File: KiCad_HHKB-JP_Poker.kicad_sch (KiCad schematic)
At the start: 21 parts, among them SW1 SW_Push, U1 ATmega32U4-MU, U2 PRTR5V0U2X, Y1 16MHz

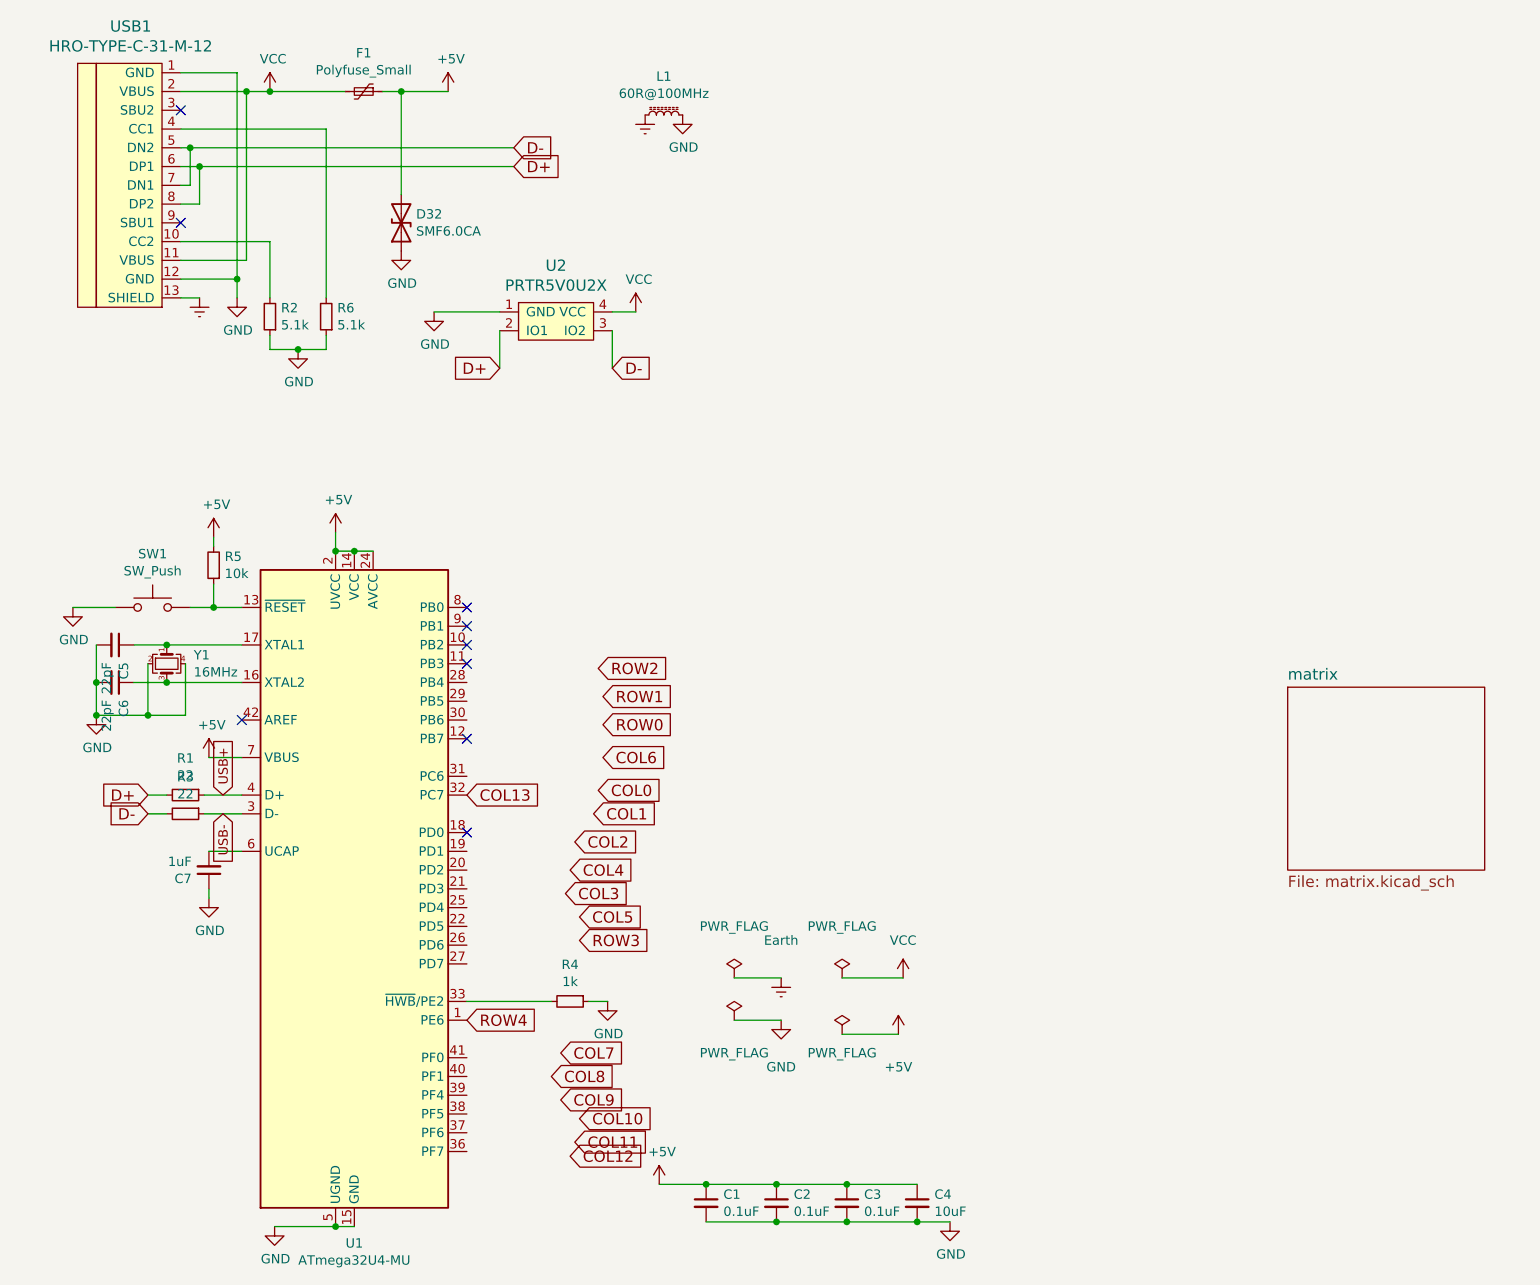
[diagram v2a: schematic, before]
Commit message: 縦（Col）の配線完了
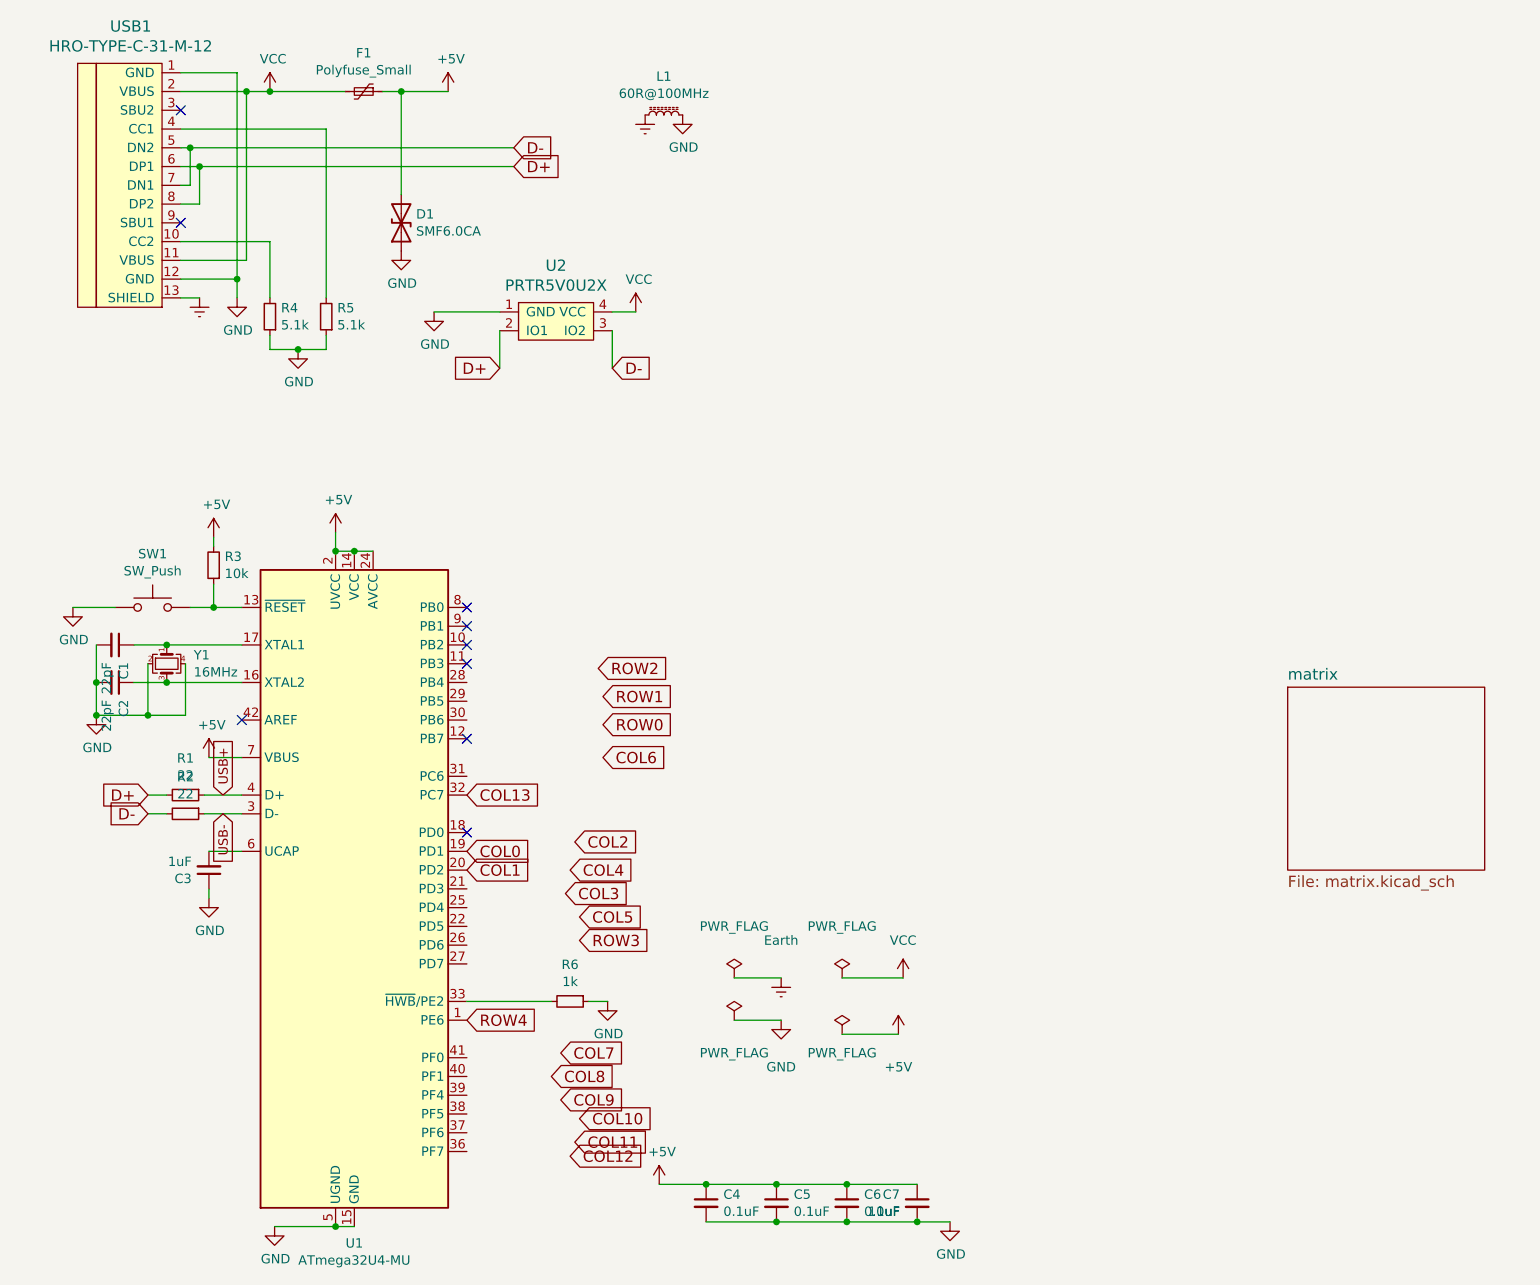
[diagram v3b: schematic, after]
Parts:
- renumbered C5 to C1, C6 to C2, C7 to C3, C1 to C4, C2 to C5, C3 to C6, C4 to C7, D32 to D1, R3 to R2, R5 to R3, R2 to R4, R6 to R5, R4 to R6
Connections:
- net COL0: now also U1.19 (PD1)
- net COL1: now also U1.20 (PD2)

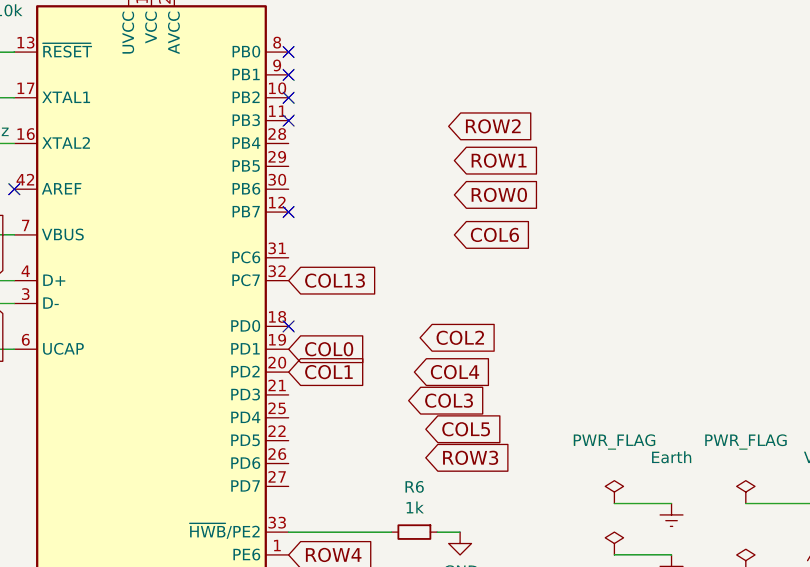
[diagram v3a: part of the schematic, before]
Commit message: key switch 間の配線は完了。これから、Key Switch と MCUを使う
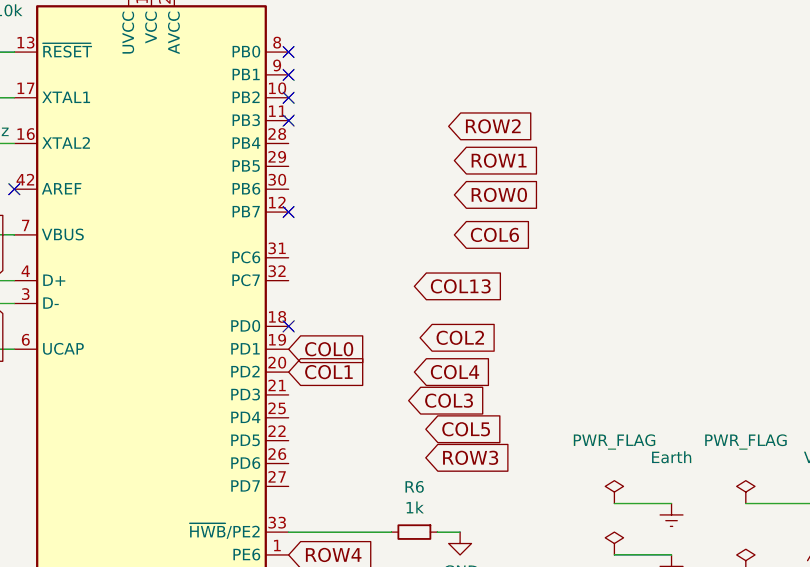
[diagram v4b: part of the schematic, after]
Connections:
- net COL13: no longer U1.32 (PC7)
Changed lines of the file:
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@@
     )
   )
-  (global_label "COL13" (shape input) (at 76.2 124.46 0) (fields_autoplaced)
+  (global_label "COL13" (shape input) (at 90.17 125.095 0) (fields_autoplaced)
     (effects (font (size 1.524 1.524)) (justify left))
-    (property "Intersheet References" "${INTERSHEET_REFS}" (id 0) (at 0 0 0)
+    (property "Intersheet References" "${INTERSHEET_REFS}" (id 0) (at 13.97 0.635 0)
       (effects (font (size 1.27 1.27)) hide)
     )

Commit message: 配線完了（検算はこれから）
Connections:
- net COL10: now also U1.29 (PB5)
- net COL11: now also U1.32 (PC7)
- net COL12: now also U1.31 (PC6)
- net COL13: now also U1.30 (PB6)
- net COL2: now also U1.41 (PF0)
- net COL3: now also U1.40 (PF1)
- net COL4: now also U1.39 (PF4)
- net COL5: now also U1.38 (PF5)
- net COL6: now also U1.37 (PF6)
- net COL7: now also U1.36 (PF7)
- net COL8: now also U1.27 (PD7)
- net COL9: now also U1.28 (PB4)
- net ROW0: now also U1.26 (PD6)
- net ROW1: now also U1.25 (PD4)
- net ROW2: now also U1.22 (PD5)
- net ROW3: now also U1.21 (PD3)
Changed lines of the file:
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@@
     )
   )
-  (global_label "ROW2" (shape input) (at 93.98 107.315 0) (fields_autoplaced)
+  (global_label "ROW2" (shape input) (at 76.2 142.24 0) (fields_autoplaced)
     (effects (font (size 1.524 1.524)) (justify left))
-    (property "Intersheet References" "${INTERSHEET_REFS}" (id 0) (at 17.78 -1.905 0)
+    (property "Intersheet References" "${INTERSHEET_REFS}" (id 0) (at 0 33.02 0)
       (effects (font (size 1.27 1.27)) hide)
     )
   )
-  (global_label "COL6" (shape input) (at 94.615 119.38 0) (fields_autoplaced)
+  (global_label "COL6" (shape input) (at 76.2 170.18 0) (fields_autoplaced)
     (effects (font (size 1.524 1.524)) (justify left))
-    (property "Intersheet References" "${INTERSHEET_REFS}" (id 0) (at 18.415 -2.54 0)
+    (property "Intersheet References" "${INTERSHEET_REFS}" (id 0) (at 0 48.26 0)
       (effects (font (size 1.27 1.27)) hide)
     )
   )
-  (global_label "COL13" (shape input) (at 90.17 125.095 0) (fields_autoplaced)
+  (global_label "COL13" (shape input) (at 76.2 114.3 0) (fields_autoplaced)
     (effects (font (size 1.524 1.524)) (justify left))
-    (property "Intersheet References" "${INTERSHEET_REFS}" (id 0) (at 13.97 0.635 0)
+    (property "Intersheet References" "${INTERSHEET_REFS}" (id 0) (at 0 -10.16 0)
       (effects (font (size 1.27 1.27)) hide)
     )
@@
     )
   )
-  (global_label "COL4" (shape input) (at 90.17 134.62 0) (fields_autoplaced)
+  (global_label "COL4" (shape input) (at 76.2 165.1 0) (fields_autoplaced)
     (effects (font (size 1.524 1.524)) (justify left))
-    (property "Intersheet References" "${INTERSHEET_REFS}" (id 0) (at 13.97 -5.08 0)
+    (property "Intersheet References" "${INTERSHEET_REFS}" (id 0) (at 0 25.4 0)
       (effects (font (size 1.27 1.27)) hide)
     )
   )
-  (global_label "ROW0" (shape input) (at 94.615 114.935 0) (fields_autoplaced)
+  (global_label "ROW0" (shape input) (at 76.2 144.78 0) (fields_autoplaced)
     (effects (font (size 1.524 1.524)) (justify left))
-    (property "Intersheet References" "${INTERSHEET_REFS}" (id 0) (at 18.415 0.635 0)
+    (property "Intersheet References" "${INTERSHEET_REFS}" (id 0) (at 0 30.48 0)
       (effects (font (size 1.27 1.27)) hide)
     )
@@
     )
   )
-  (global_label "COL3" (shape input) (at 89.535 137.795 0) (fields_autoplaced)
+  (global_label "COL3" (shape input) (at 76.2 162.56 0) (fields_autoplaced)
     (effects (font (size 1.524 1.524)) (justify left))
-    (property "Intersheet References" "${INTERSHEET_REFS}" (id 0) (at 13.335 -4.445 0)
+    (property "Intersheet References" "${INTERSHEET_REFS}" (id 0) (at 0 20.32 0)
       (effects (font (size 1.27 1.27)) hide)
     )
   )
-  (global_label "ROW3" (shape input) (at 91.44 144.145 0) (fields_autoplaced)
+  (global_label "ROW3" (shape input) (at 76.2 137.16 0) (fields_autoplaced)
     (effects (font (size 1.524 1.524)) (justify left))
-    (property "Intersheet References" "${INTERSHEET_REFS}" (id 0) (at 15.24 -3.175 0)
+    (property "Intersheet References" "${INTERSHEET_REFS}" (id 0) (at 0 -10.16 0)
       (effects (font (size 1.27 1.27)) hide)
     )
   )
-  (global_label "COL8" (shape input) (at 87.63 162.56 0) (fields_autoplaced)
+  (global_label "COL8" (shape input) (at 76.2 147.32 0) (fields_autoplaced)
     (effects (font (size 1.524 1.524)) (justify left))
-    (property "Intersheet References" "${INTERSHEET_REFS}" (id 0) (at 11.43 0 0)
+    (property "Intersheet References" "${INTERSHEET_REFS}" (id 0) (at 0 -15.24 0)
       (effects (font (size 1.27 1.27)) hide)
     )
   )
-  (global_label "COL12" (shape input) (at 90.17 173.355 0) (fields_autoplaced)
+  (global_label "COL12" (shape input) (at 76.2 121.92 0) (fields_autoplaced)
     (effects (font (size 1.524 1.524)) (justify left))
-    (property "Intersheet References" "${INTERSHEET_REFS}" (id 0) (at 13.97 0.635 0)
+    (property "Intersheet References" "${INTERSHEET_REFS}" (id 0) (at 0 -50.8 0)
       (effects (font (size 1.27 1.27)) hide)
     )
   )
-  (global_label "COL5" (shape input) (at 91.44 140.97 0) (fields_autoplaced)
+  (global_label "COL5" (shape input) (at 76.2 167.64 0) (fields_autoplaced)
     (effects (font (size 1.524 1.524)) (justify left))
-    (property "Intersheet References" "${INTERSHEET_REFS}" (id 0) (at 15.24 -3.81 0)
+    (property "Intersheet References" "${INTERSHEET_REFS}" (id 0) (at 0 22.86 0)
       (effects (font (size 1.27 1.27)) hide)
     )
   )
-  (global_label "COL7" (shape input) (at 88.9 159.385 0) (fields_autoplaced)
+  (global_label "COL7" (shape input) (at 76.2 172.72 0) (fields_autoplaced)
     (effects (font (size 1.524 1.524)) (justify left))
-    (property "Intersheet References" "${INTERSHEET_REFS}" (id 0) (at 12.7 -0.635 0)
+    (property "Intersheet References" "${INTERSHEET_REFS}" (id 0) (at 0 12.7 0)
       (effects (font (size 1.27 1.27)) hide)
     )
   )
-  (global_label "COL9" (shape input) (at 88.9 165.735 0) (fields_autoplaced)
+  (global_label "COL9" (shape input) (at 76.2 109.22 0) (fields_autoplaced)
     (effects (font (size 1.524 1.524)) (justify left))
-    (property "Intersheet References" "${INTERSHEET_REFS}" (id 0) (at 12.7 0.635 0)
+    (property "Intersheet References" "${INTERSHEET_REFS}" (id 0) (at 0 -55.88 0)
       (effects (font (size 1.27 1.27)) hide)
     )
@@
     )
   )
-  (global_label "COL2" (shape input) (at 90.805 130.81 0) (fields_autoplaced)
+  (global_label "COL2" (shape input) (at 76.2 160.02 0) (fields_autoplaced)
     (effects (font (size 1.524 1.524)) (justify left))
-    (property "Intersheet References" "${INTERSHEET_REFS}" (id 0) (at 14.605 -6.35 0)
+    (property "Intersheet References" "${INTERSHEET_REFS}" (id 0) (at 0 22.86 0)
       (effects (font (size 1.27 1.27)) hide)
     )
@@
     )
   )
-  (global_label "COL10" (shape input) (at 91.44 168.275 0) (fields_autoplaced)
+  (global_label "COL10" (shape input) (at 76.2 111.76 0) (fields_autoplaced)
     (effects (font (size 1.524 1.524)) (justify left))
-    (property "Intersheet References" "${INTERSHEET_REFS}" (id 0) (at 15.24 0.635 0)
+    (property "Intersheet References" "${INTERSHEET_REFS}" (id 0) (at 0 -55.88 0)
       (effects (font (size 1.27 1.27)) hide)
     )
   )
-  (global_label "COL11" (shape input) (at 90.805 171.45 0) (fields_autoplaced)
+  (global_label "COL11" (shape input) (at 76.2 124.46 0) (fields_autoplaced)
     (effects (font (size 1.524 1.524)) (justify left))
-    (property "Intersheet References" "${INTERSHEET_REFS}" (id 0) (at 14.605 1.27 0)
+    (property "Intersheet References" "${INTERSHEET_REFS}" (id 0) (at 0 -45.72 0)
       (effects (font (size 1.27 1.27)) hide)
     )
   )
-  (global_label "ROW1" (shape input) (at 94.615 111.125 0) (fields_autoplaced)
+  (global_label "ROW1" (shape input) (at 76.2 139.7 0) (fields_autoplaced)
     (effects (font (size 1.524 1.524)) (justify left))
-    (property "Intersheet References" "${INTERSHEET_REFS}" (id 0) (at 18.415 -0.635 0)
+    (property "Intersheet References" "${INTERSHEET_REFS}" (id 0) (at 0 27.94 0)
       (effects (font (size 1.27 1.27)) hide)
     )
